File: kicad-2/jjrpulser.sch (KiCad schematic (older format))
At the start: 21 parts, among them J1 Conn_Coaxial_Power, J3 Screw_Terminal_HOT, J4 Screw_Terminal_COLD, J5 Conn_UART, U1 ESP-12, U2 AMS1117-3.3_SOT223

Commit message: Новая разводка
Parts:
- added R12, R13, R14: 470, Resistors_SMD:R_0805_HandSoldering, symbol R
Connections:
- net at R11.2, R2.1, U1.1 (REST): now also R14.1; no longer J5.1 (Pin_1)
- net at U1.15 (RXD): now also R13.2; no longer J5.4 (Pin_4)
- net at U1.16 (TXD): now also R12.1; no longer J5.3 (Pin_3)
- new net: J5.1 (Pin_1), R14.2
- new net: J5.3 (Pin_3), R12.2
- new net: J5.4 (Pin_4), R13.1
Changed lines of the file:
@@
 	6600 4100 6600 4400
 Wire Wire Line
-	6600 3600 7950 3600
-Wire Wire Line
-	6600 3500 7950 3500
-Wire Wire Line
 	4350 3700 4800 3700
 Wire Wire Line
@@
 Wire Wire Line
 	4800 2700 7950 2700
-Wire Wire Line
-	7950 2700 7950 3300
 Wire Wire Line
 	6600 4000 6800 4000
@@
 	4500 3800 4500 3500
 Connection ~ 4500 3500
+$Comp
+L R R14
+U 1 1 5D0C1CEE
+P 7950 3150
+F 0 "R14" V 8030 3150 50  0000 C CNN
+F 1 "470" V 7950 3150 50  0000 C CNN
+F 2 "Resistors_SMD:R_0805_HandSoldering" V 7880 3150 50  0001 C CNN
+F 3 "" H 7950 3150 50  0001 C CNN
+	1    7950 3150
+	1    0    0    -1
+$EndComp
+Wire Wire Line
+	7950 2700 7950 3000
+$Comp
+L R R12
+U 1 1 5D0C1EF1
+P 7350 3500
+F 0 "R12" V 7430 3500 50  0000 C CNN
+F 1 "470" V 7350 3500 50  0000 C CNN
+F 2 "Resistors_SMD:R_0805_HandSoldering" V 7280 3500 50  0001 C CNN
+F 3 "" H 7350 3500 50  0001 C CNN
+	1    7350 3500
+	0    -1   -1   0
+$EndComp
+$Comp
+L R R13
+U 1 1 5D0C1FC2
+P 7350 3600
+F 0 "R13" V 7430 3600 50  0000 C CNN
+F 1 "470" V 7350 3600 50  0000 C CNN
+F 2 "Resistors_SMD:R_0805_HandSoldering" V 7280 3600 50  0001 C CNN
+F 3 "" H 7350 3600 50  0001 C CNN
+	1    7350 3600
+	0    1    1    0
+$EndComp
+Wire Wire Line
+	6600 3500 7200 3500
+Wire Wire Line
+	7500 3500 7950 3500
+Wire Wire Line
+	6600 3600 7200 3600
+Wire Wire Line
+	7500 3600 7950 3600
 $EndSCHEMATC

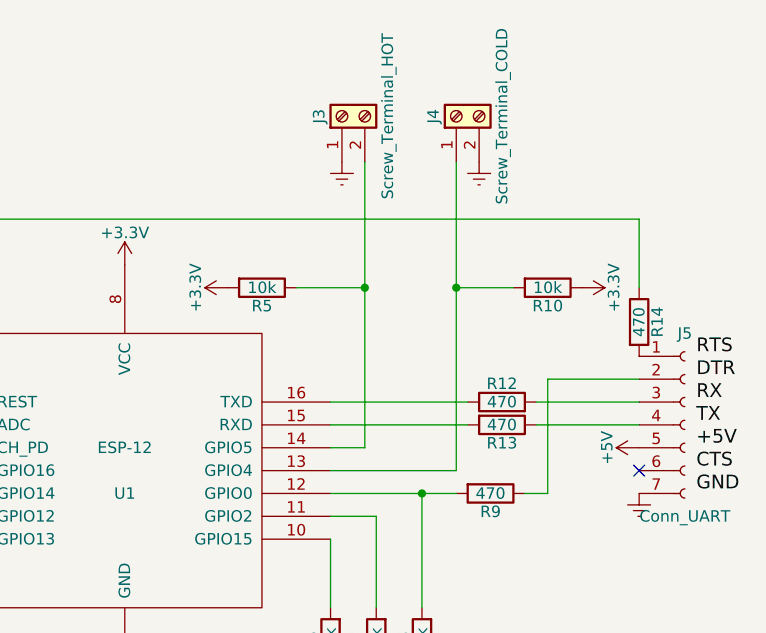
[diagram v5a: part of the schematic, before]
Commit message: Разводка2: Защитные резисторы на подключении водосчетчиков
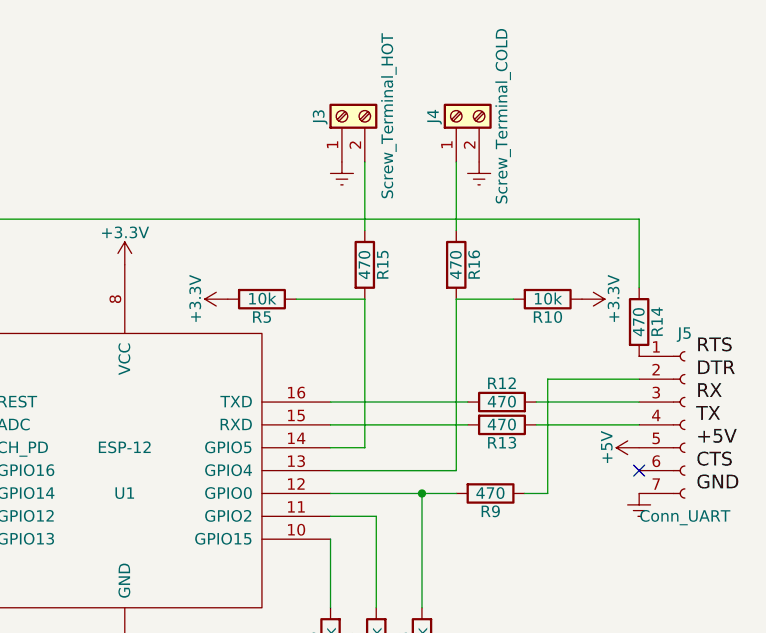
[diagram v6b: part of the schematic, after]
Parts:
- added R15, R16: 470, Resistors_SMD:R_0805_HandSoldering, symbol R
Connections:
- net at R10.2, U1.13 (GPIO4): now also R16.2; no longer J4.1 (Pin_1)
- net at R5.1, U1.14 (GPIO5): now also R15.2; no longer J3.2 (Pin_2)
- new net: J4.1 (Pin_1), R16.1
- new net: J3.2 (Pin_2), R15.1
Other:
- moved on the sheet: R10, R5

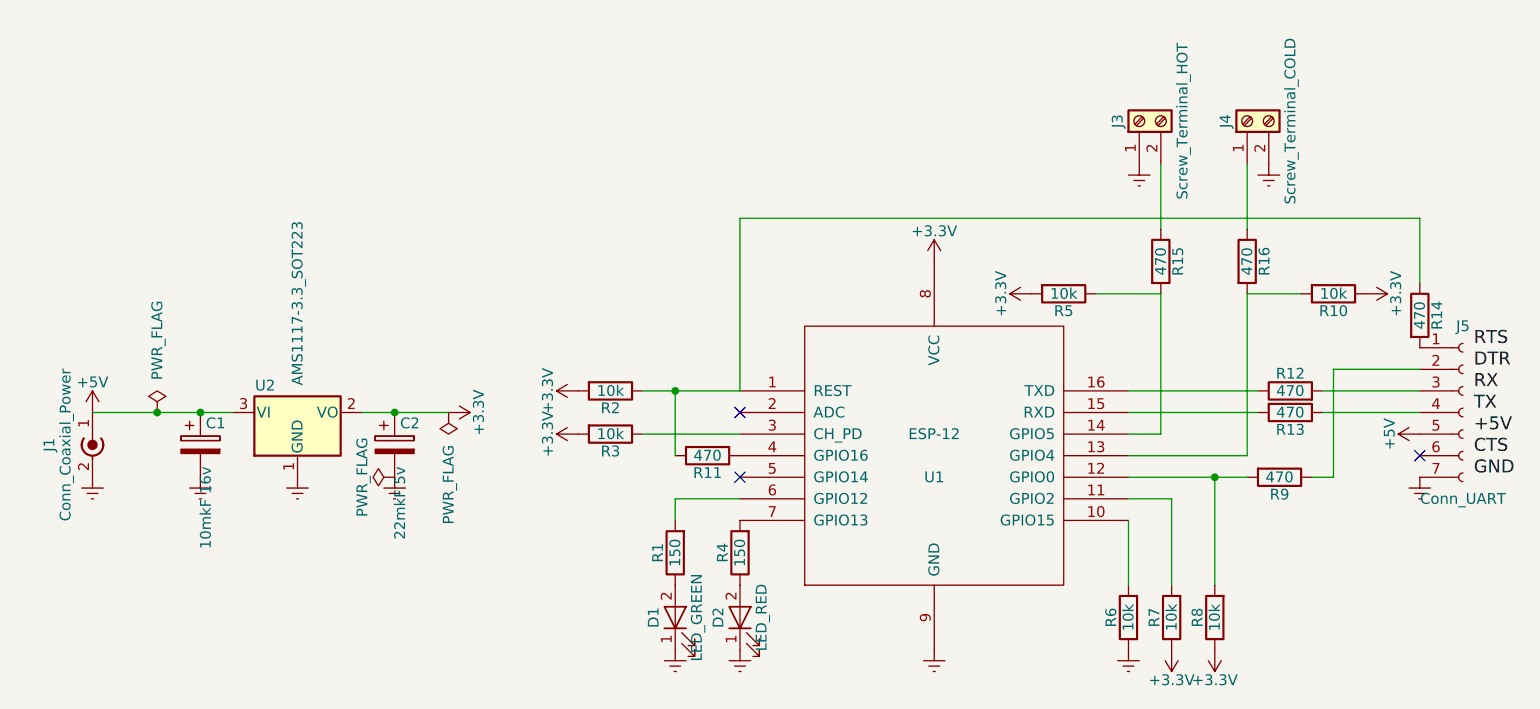
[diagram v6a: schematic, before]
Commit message: Новые маленькие коннекторы для счетчиков и питания
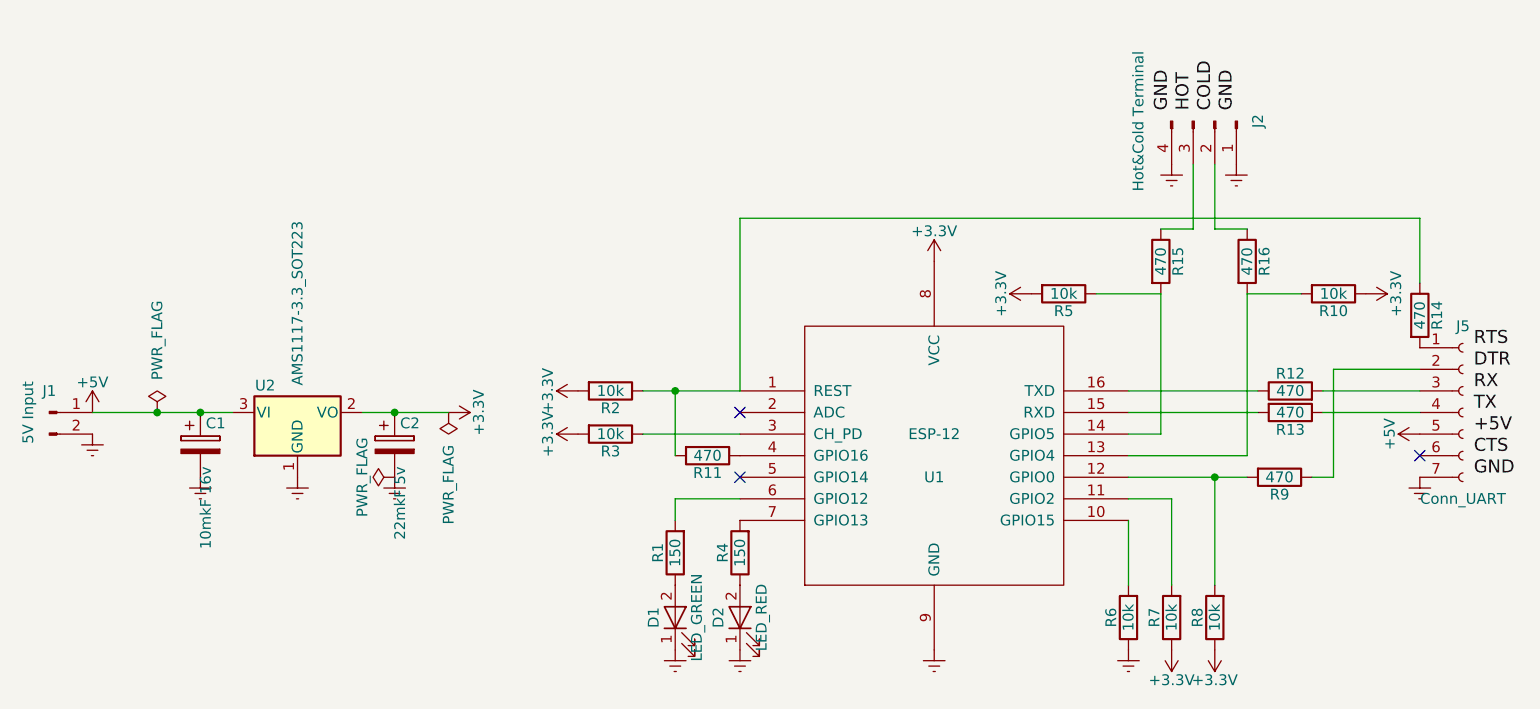
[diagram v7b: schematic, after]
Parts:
- removed J1: Conn_Coaxial_Power, Connectors_TE-Connectivity:BNC_Socket_TYCO-AMP_LargePads, symbol Conn_Coaxial_Power
- removed J3: Screw_Terminal_HOT, Connectors_Terminal_Blocks:TerminalBlock_Pheonix_MPT-2.54mm_2pol, symbol Screw_Terminal_01x02
- removed J4: Screw_Terminal_COLD, Connectors_Terminal_Blocks:TerminalBlock_Pheonix_MPT-2.54mm_2pol, symbol Screw_Terminal_01x02
- added J1: 5V Input, Connectors_JST:JST_PH_S2B-PH-K_02x2.00mm_Angled, symbol Conn_01x02_Male
- added J2: Hot&Cold Terminal, Connectors_JST:JST_PH_S4B-PH-K_04x2.00mm_Angled, symbol Conn_01x04_Male
- C1, C2: footprint Capacitors_SMD:CP_Elec_6.3x5.3 -> Capacitors_Tantalum_SMD:CP_Tantalum_Case-A_EIA-3216-18_Reflow
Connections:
- net +5V: now also J1.1 (Pin_1)
- net Earth: now also J1.2 (Pin_2), J2.1 (Pin_1), J2.4 (Pin_4)
- net at R16.1: now also J2.2 (Pin_2)
- net at R15.1: now also J2.3 (Pin_3)
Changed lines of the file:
@@
-$EndComp
-$Comp
-L Screw_Terminal_01x02 J4
-U 1 1 5CBBAB1E
-P 7150 2250
-F 0 "J4" H 7150 2350 50  0000 C CNN
-F 1 "Screw_Terminal_COLD" H 7150 2050 50  0000 C CNN
-F 2 "Connectors_Terminal_Blocks:TerminalBlock_Pheonix_MPT-2.54mm_2pol" H 7150 2250 50  0001 C CNN
-F 3 "" H 7150 2250 50  0001 C CNN
-	1    7150 2250
-	0    -1   -1   0
-$EndComp
-$Comp
-L Screw_Terminal_01x02 J3
-U 1 1 5CBBDEAC
-P 6650 2250
-F 0 "J3" H 6650 2350 50  0000 C CNN
-F 1 "Screw_Terminal_HOT" H 6650 2050 50  0000 C CNN
-F 2 "Connectors_Terminal_Blocks:TerminalBlock_Pheonix_MPT-2.54mm_2pol" H 6650 2250 50  0001 C CNN
-F 3 "" H 6650 2250 50  0001 C CNN
-	1    6650 2250
-	0    -1   -1   0
 $EndComp
 $Comp
 L Earth #PWR015
 U 1 1 5CBC9513
-P 7250 2450
-F 0 "#PWR015" H 7250 2200 50  0001 C CNN
-F 1 "Earth" H 7250 2300 50  0001 C CNN
-F 2 "" H 7250 2450 50  0001 C CNN
-F 3 "" H 7250 2450 50  0001 C CNN
-	1    7250 2450
+P 7100 2450
+F 0 "#PWR015" H 7100 2200 50  0001 C CNN
+F 1 "Earth" H 7100 2300 50  0001 C CNN
+F 2 "" H 7100 2450 50  0001 C CNN
+F 3 "" H 7100 2450 50  0001 C CNN
+	1    7100 2450
 	1    0    0    -1
 $EndComp
@@
 L Earth #PWR016
 U 1 1 5CBC956E
-P 6650 2450
-F 0 "#PWR016" H 6650 2200 50  0001 C CNN
-F 1 "Earth" H 6650 2300 50  0001 C CNN
-F 2 "" H 6650 2450 50  0001 C CNN
-F 3 "" H 6650 2450 50  0001 C CNN
-	1    6650 2450
+P 6800 2450
+F 0 "#PWR016" H 6800 2200 50  0001 C CNN
+F 1 "Earth" H 6800 2300 50  0001 C CNN
+F 2 "" H 6800 2450 50  0001 C CNN
+F 3 "" H 6800 2450 50  0001 C CNN
+	1    6800 2450
 	1    0    0    -1
 $EndComp
@@
 F 0 "C1" H 2325 3850 50  0000 L CNN
 F 1 "10mkF 16v" V 2325 3650 50  0000 R CNN
-F 2 "Capacitors_SMD:CP_Elec_6.3x5.3" H 2338 3600 50  0001 C CNN
+F 2 "Capacitors_Tantalum_SMD:CP_Tantalum_Case-A_EIA-3216-18_Reflow" H 2338 3600 50  0001 C CNN
 F 3 "" H 2300 3750 50  0001 C CNN
 	1    2300 3750
@@
 L Earth #PWR018
 U 1 1 5D018FC9
-P 1800 3900
-F 0 "#PWR018" H 1800 3650 50  0001 C CNN
-F 1 "Earth" H 1800 3750 50  0001 C CNN
-F 2 "" H 1800 3900 50  0001 C CNN
-F 3 "" H 1800 3900 50  0001 C CNN
-	1    1800 3900
+P 1800 3700
+F 0 "#PWR018" H 1800 3450 50  0001 C CNN
+F 1 "Earth" H 1800 3550 50  0001 C CNN
+F 2 "" H 1800 3700 50  0001 C CNN
+F 3 "" H 1800 3700 50  0001 C CNN
+	1    1800 3700
 	1    0    0    -1
 $EndComp
@@
 F 0 "C2" H 3225 3850 50  0000 L CNN
 F 1 "22mkF 5v" V 3225 3650 50  0000 R CNN
-F 2 "Capacitors_SMD:CP_Elec_6.3x5.3" H 3238 3600 50  0001 C CNN
+F 2 "Capacitors_Tantalum_SMD:CP_Tantalum_Case-A_EIA-3216-18_Reflow" H 3238 3600 50  0001 C CNN
 F 3 "" H 3200 3750 50  0001 C CNN
 	1    3200 3750
@@
 F 3 "" H 2100 3600 50  0001 C CNN
 	1    2100 3600
-	1    0    0    -1
-$EndComp
-$Comp
-L Conn_Coaxial_Power J1
-U 1 1 5D07B797
-P 1800 3700
-F 0 "J1" V 1600 3650 50  0000 C CNN
-F 1 "Conn_Coaxial_Power" V 1675 3650 50  0000 C CNN
-F 2 "Connectors_TE-Connectivity:BNC_Socket_TYCO-AMP_LargePads" H 1800 3650 50  0001 C CNN
-F 3 "" H 1800 3650 50  0001 C CNN
-	1    1800 3700
 	1    0    0    -1
 $EndComp
@@
 $EndComp
 Wire Wire Line
-	6750 2750 6750 2450
-Wire Wire Line
-	7150 2750 7150 2450
-Wire Wire Line
 	6450 3050 6750 3050
 Wire Wire Line
@@
 Wire Wire Line
 	7150 3800 7150 3050
+Text Label 6800 2200 1    60   ~ 0
+GND
+Text Label 6900 2200 1    60   ~ 0
+HOT
+Text Label 7000 2200 1    60   ~ 0
+COLD
+Text Label 7100 2200 1    60   ~ 0
+GND
+Wire Wire Line
+	6750 2750 6900 2750
+Wire Wire Line
+	6900 2750 6900 2450
+Wire Wire Line
+	7150 2750 7000 2750
+Wire Wire Line
+	7000 2750 7000 2450
+$Comp
+L Conn_01x04_Male J2
+U 1 1 5D154AC3
+P 7000 2250
+F 0 "J2" H 7000 2450 50  0000 C CNN
+F 1 "Hot&Cold Terminal" H 7000 1896 50  0000 C CNN
+F 2 "Connectors_JST:JST_PH_S4B-PH-K_04x2.00mm_Angled" H 7000 2250 50  0001 C CNN
+F 3 "" H 7000 2250 50  0001 C CNN
+	1    7000 2250
+	0    1    1    0
+$EndComp
+$Comp
+L Conn_01x02_Male J1
+U 1 1 5D156AD5
+P 1600 3600
+F 0 "J1" H 1600 3700 50  0000 C CNN
+F 1 "5V Input" V 1502 3600 50  0000 C CNN
+F 2 "Connectors_JST:JST_PH_S2B-PH-K_02x2.00mm_Angled" H 1600 3600 50  0001 C CNN
+F 3 "" H 1600 3600 50  0001 C CNN
+	1    1600 3600
+	1    0    0    -1
+$EndComp
 $EndSCHEMATC
